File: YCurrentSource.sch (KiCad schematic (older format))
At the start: 28 parts, among them Q10 MMBT3906, Q11 MMBT3904, Q12 MMBT3906, Q13 MMBT3904, Q14 MMBFJ309, Q8 MMBT3906, Q9 MMBT3904, U9 LM358

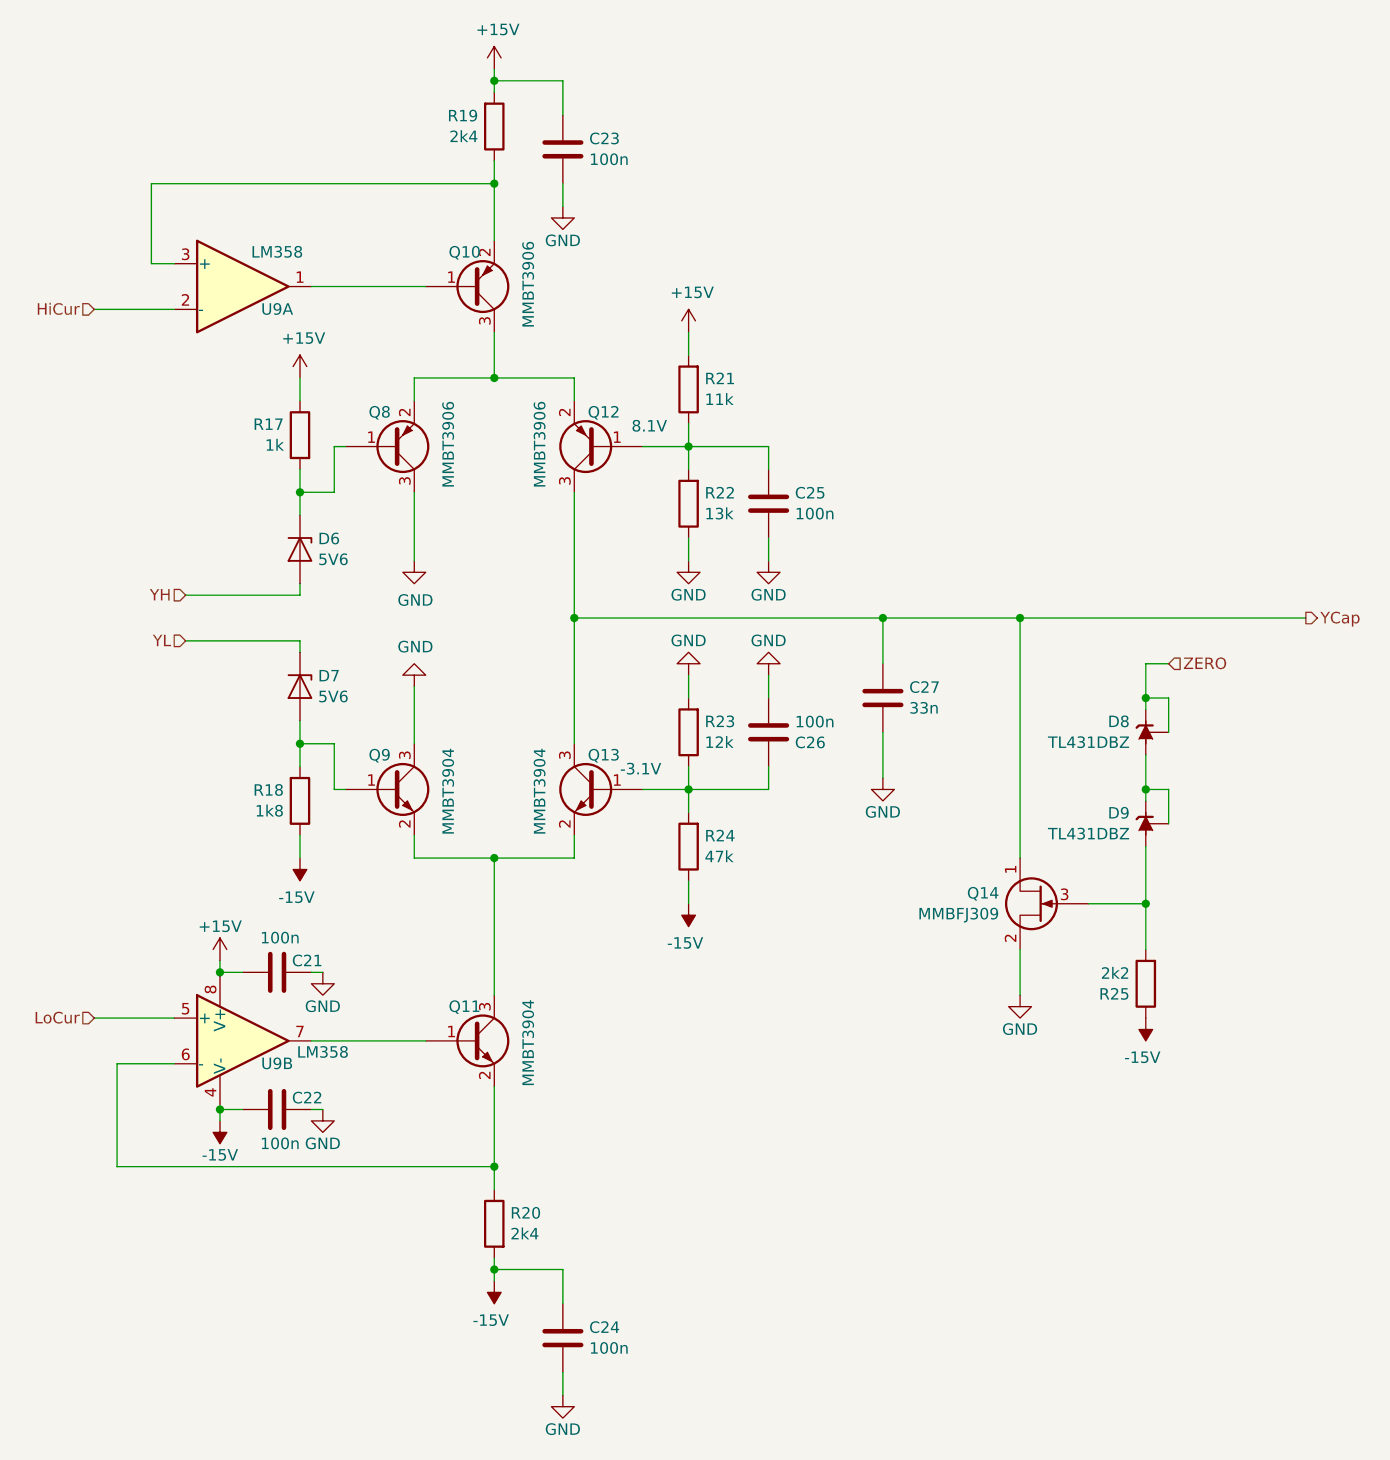
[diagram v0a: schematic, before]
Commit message: Fixed some bugs, finished block symbols
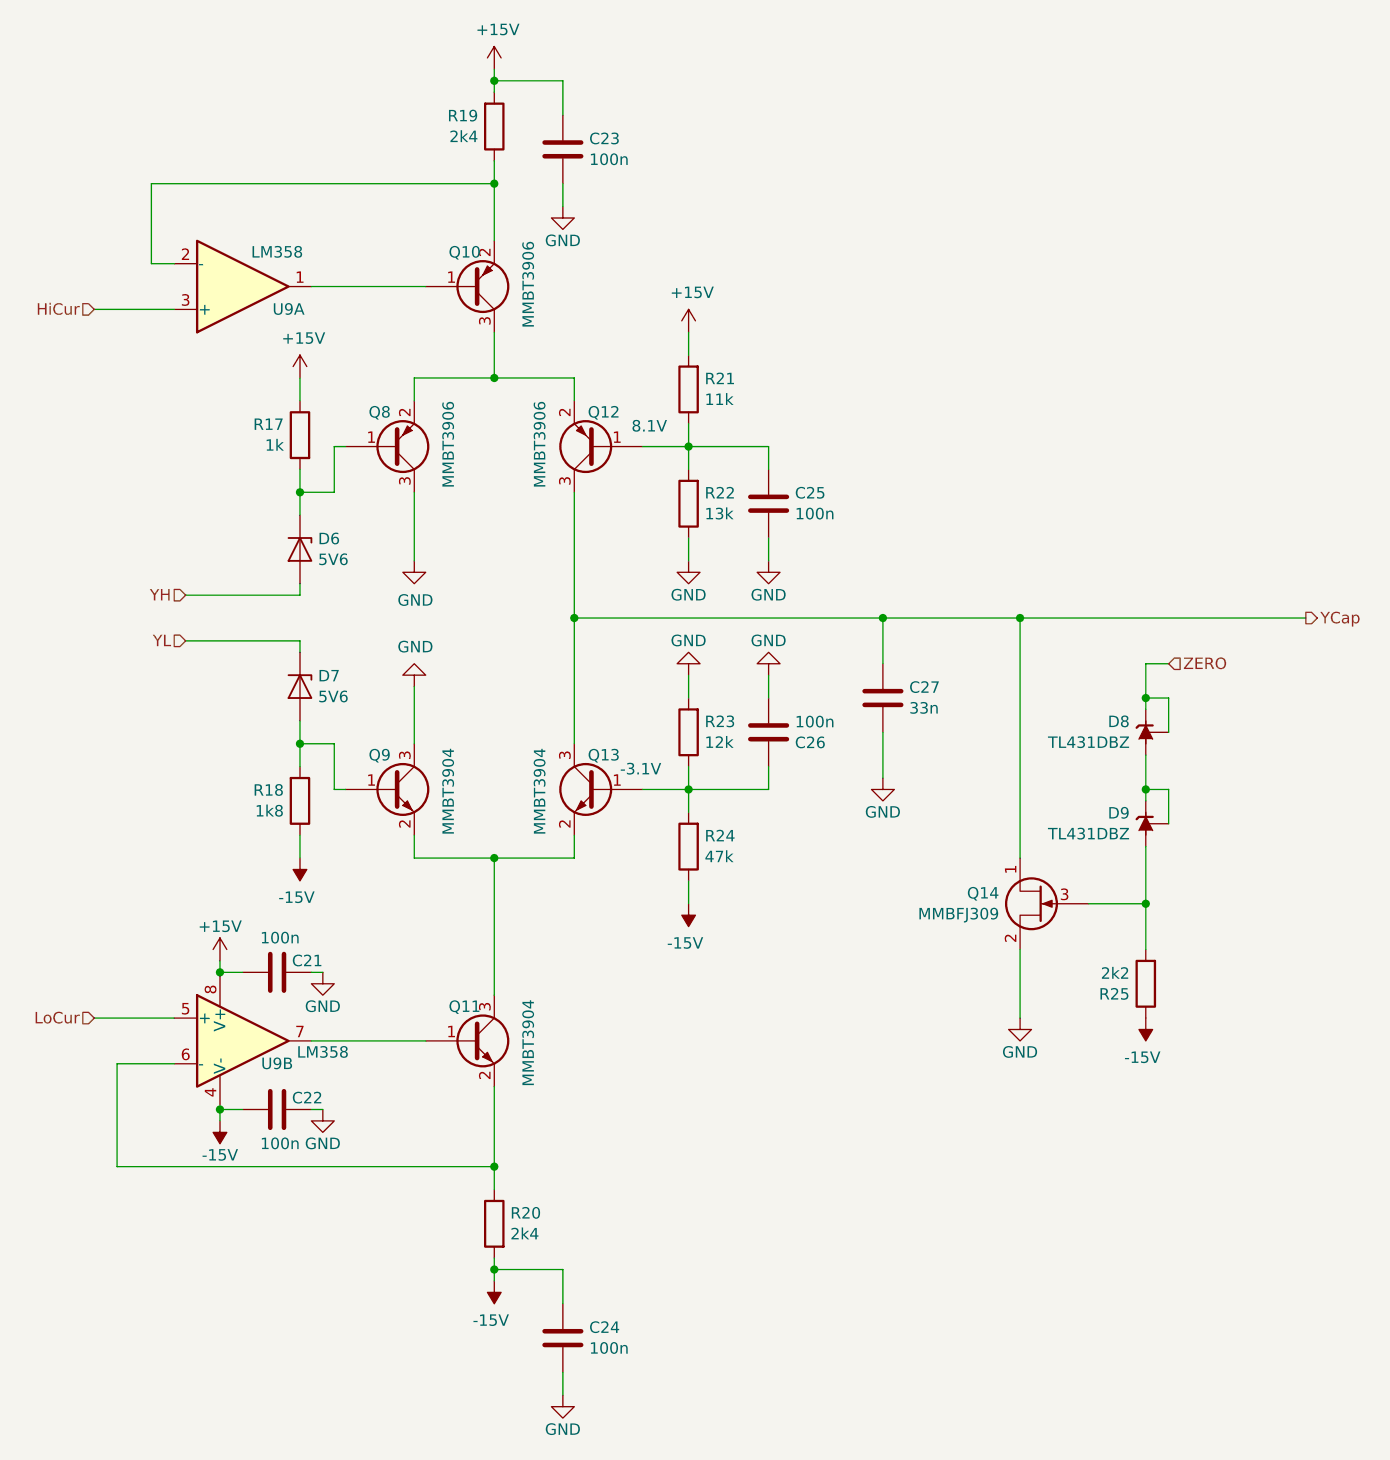
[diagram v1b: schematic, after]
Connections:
- net HiCur: now also U9.3 (+); no longer U9.2 (-)
- net at Q10.2 (E), R19.1: now also U9.2 (-); no longer U9.3 (+)
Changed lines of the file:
@@
 encoding utf-8
 Sheet 8 13
-Title ""
-Date ""
-Rev ""
-Comp ""
-Comment1 ""
+Title "Y Current Source"
+Date "2021-04-20"
+Rev "2.0"
+Comp "Filip Piórski"
+Comment1 "Charges/discharges/leaves the signal cap alone"
 Comment2 ""
 Comment3 ""
@@
 AR Path="/601DE80D/60394DA6/6062A92D" Ref="U?"  Part="1"
 AR Path="/601E8CD6/6062A92D" Ref="U9"  Part="1"
-F 0 "U9" H 3650 2050 50  0000 C CNN
-F 1 "LM358" H 3650 2300 50  0000 C CNN
+F 0 "U9" H 3700 2250 50  0000 C CNN
+F 1 "LM358" H 3650 2000 50  0000 C CNN
 F 2 "Package_SO:SOIC-8_3.9x4.9mm_P1.27mm" H 3500 2150 50  0001 C CNN
 F 3 "http://www.ti.com/lit/ds/symlink/lm2904-n.pdf" H 3500 2150 50  0001 C CNN
 	1    3500 2150
-	1    0    0    -1
+	1    0    0    1
 $EndComp
 $Comp
@@
 	4250 3900 4250 4150
 Wire Wire Line
-	6900 5250 6900 5050
+	6900 5350 6900 5050
 $Comp
 L power:GND #PWR?
 U 1 1 6025F41B
-P 6900 5250
+P 6900 5350
 AR Path="/5FA4B51C/6025F41B" Ref="#PWR?"  Part="1"
 AR Path="/601DE80D/6025F41B" Ref="#PWR?"  Part="1"
@@
 AR Path="/601DE80D/60394DA6/6025F41B" Ref="#PWR?"  Part="1"
 AR Path="/601E8CD6/6025F41B" Ref="#PWR0114"  Part="1"
-F 0 "#PWR0114" H 6900 5000 50  0001 C CNN
-F 1 "GND" H 6900 5100 50  0000 C CNN
-F 2 "" H 6900 5250 50  0001 C CNN
-F 3 "" H 6900 5250 50  0001 C CNN
-	1    6900 5250
-	-1   0    0    -1
-$EndComp
+F 0 "#PWR0114" H 6900 5100 50  0001 C CNN
+F 1 "GND" H 6900 5200 50  0000 C CNN
+F 2 "" H 6900 5350 50  0001 C CNN
+F 3 "" H 6900 5350 50  0001 C CNN
+	1    6900 5350
+	-1   0    0    -1
+$EndComp
